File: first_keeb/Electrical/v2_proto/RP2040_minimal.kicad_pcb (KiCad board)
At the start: 2 copper layers, 54.3 x 61.2 mm, 32 parts, among them P1 USB_C_Receptacle_GCT_USB4105-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, Q1 SOT-23, SW1 2-1825027-0_Right_Angle_Switc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, U1 NCP1117-3.3_SOT223, U2 W25Q128JVS, U3 RP2040, U4 128x64OLED, Y1 ABLS-12.000MHZ-B4-T

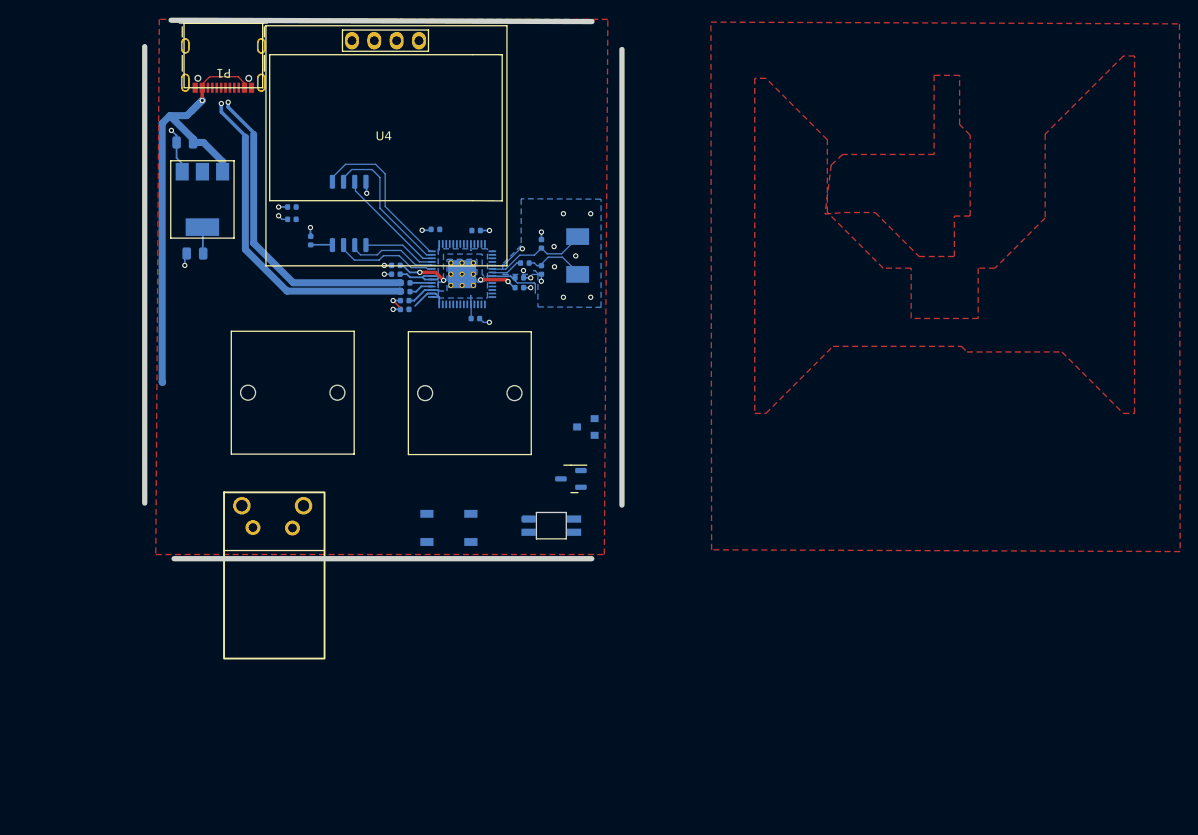
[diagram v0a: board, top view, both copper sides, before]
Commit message: finishes pcb except for the test points.
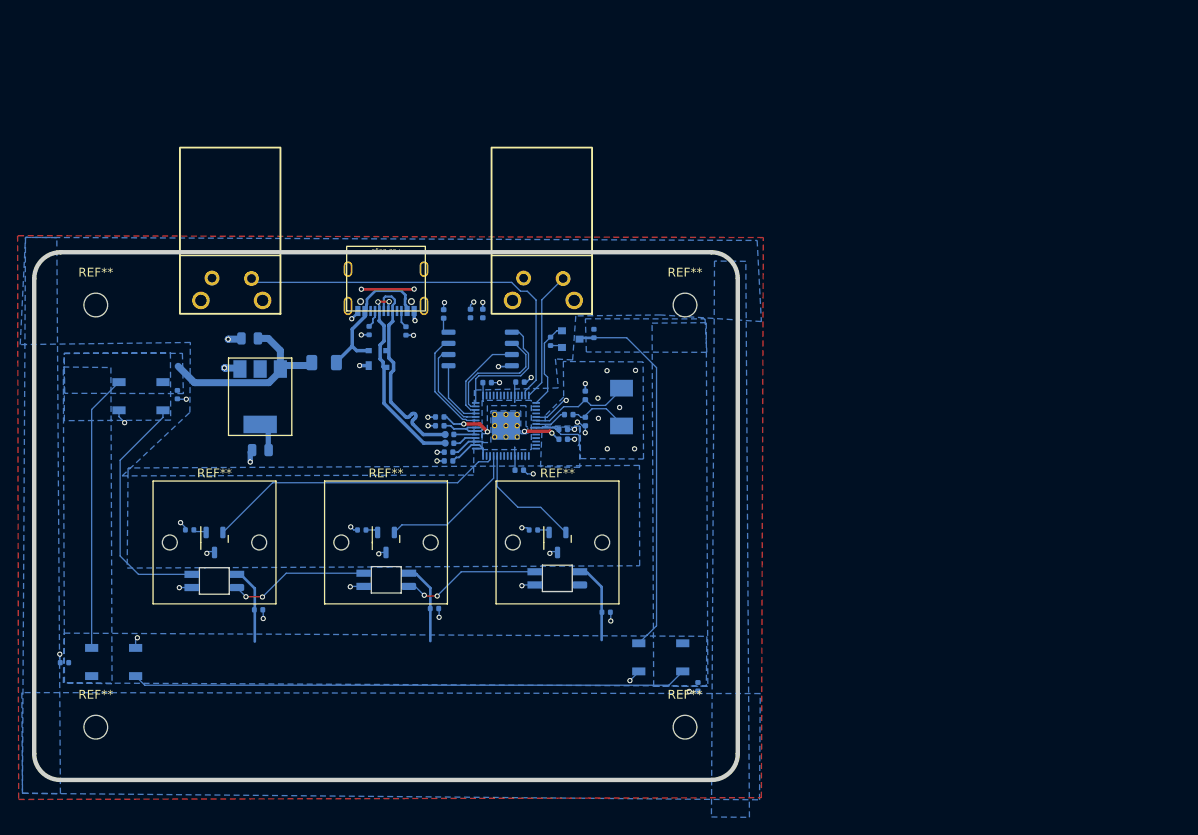
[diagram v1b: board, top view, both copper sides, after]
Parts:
- removed the REF** at (91.9, 107.9)
- removed the REF** at (112.1, 107.9)
- removed U4: 128x64OLED, SSD1306:128x64OLED
- added C19: C_0402_1005Metric, Capacitor_SMD:C_0402_1005Metric, B.Cu at (85.5, 137.7)
- added C20: C_0402_1005Metric, Capacitor_SMD:C_0402_1005Metric, B.Cu at (105.5, 137.5)
- added C21: C_0402_1005Metric, Capacitor_SMD:C_0402_1005Metric, B.Cu at (116.8, 128.6)
- added C22: C_0402_1005Metric, Capacitor_SMD:C_0402_1005Metric, B.Cu at (97.2, 128.6)
- added C23: C_0402_1005Metric, Capacitor_SMD:C_0402_1005Metric, B.Cu at (77.7, 128.6)
- added C24: C_0402_1005Metric, Capacitor_SMD:C_0402_1005Metric, B.Cu at (76.3, 113.2)
- added C25: C_0402_1005Metric, Capacitor_SMD:C_0402_1005Metric, B.Cu at (63.4, 143.7)
- added C26: C_0402_1005Metric, Capacitor_SMD:C_0402_1005Metric, B.Cu at (135.5, 146.4)
- added C28: C_0402_1005Metric, Capacitor_SMD:C_0402_1005Metric, B.Cu at (125.0, 137.9)
- added D2: SK6812-MINI-E, Keebio-Parts:SK6812-MINI-E, B.Cu at (100.0, 134.2)
- added D3: WS2812B, Keebio-Parts:WS2812B, B.Cu at (131.2, 143.1)
- added D4: WS2812B, Keebio-Parts:WS2812B, B.Cu at (69.0, 143.6)
- added D7: SK6812-MINI-E, Keebio-Parts:SK6812-MINI-E, B.Cu at (119.5, 134.1)
- added F1: Fuse_1206_3216Metric, Fuse:Fuse_1206_3216Metric, B.Cu at (93.0, 109.5)
- added R10: C_0402_1005Metric, Capacitor_SMD:C_0402_1005Metric, B.Cu at (123.6, 106.2)
- added R7: C_0402_1005Metric, Capacitor_SMD:C_0402_1005Metric, B.Cu at (98.1, 105.9)
- added R8: C_0402_1005Metric, Capacitor_SMD:C_0402_1005Metric, B.Cu at (102.3, 106.0)
- added R9: C_0402_1005Metric, Capacitor_SMD:C_0402_1005Metric, B.Cu at (118.7, 107.1)
- added REF**: SW_Lekker_MX_1.00u_PCB, Button_Switch_Keyboard:SW_Lekker_MX_1.00u_PCB, F.Cu at (80.5, 130.0)
- added REF**: SW_Lekker_MX_1.00u_PCB, Button_Switch_Keyboard:SW_Lekker_MX_1.00u_PCB, F.Cu at (119.5, 130.0)
- added REF**: SW_Lekker_MX_1.00u_PCB, Button_Switch_Keyboard:SW_Lekker_MX_1.00u_PCB, F.Cu at (100.0, 130.0)
- added REF**: MountingHole_2.7mm_M2.5, MountingHole:MountingHole_2.7mm_M2.5, F.Cu at (67.0, 103.0)
- added REF**: MountingHole_2.7mm_M2.5, MountingHole:MountingHole_2.7mm_M2.5, F.Cu at (67.0, 151.0)
- added REF**: MountingHole_2.7mm_M2.5, MountingHole:MountingHole_2.7mm_M2.5, F.Cu at (134.0, 103.0)
- added REF**: MountingHole_2.7mm_M2.5, MountingHole:MountingHole_2.7mm_M2.5, F.Cu at (134.0, 151.0)
- added S2: SS39ET, Package_TO_SOT_SMD:SOT-23-3, B.Cu at (100.0, 130.0)
- added S3: SS39ET, Package_TO_SOT_SMD:SOT-23-3, B.Cu at (80.5, 130.0)
- added SW2: 2-1825027-0_Right_Angle_Switch-9.24mm_Stem, Button_Switch_THT:2-1825027-0_Right_Angle_Button, F.Cu at (112.0, 104.0)
- added U5: SOT143B, Keebio-Parts:SOT-143B, B.Cu at (99.0, 109.1)
- P1: moved to B.Cu
- moved D1 38.8 mm to (80.5, 134.4), turned to 0 degrees
- moved D5 38.1 mm to (72.1, 113.4)
- moved P1 31.4 mm to (100.0, 100.0), turned to 0 degrees
- moved C16 24.9 mm to (111.0, 104.0), turned to 90 degrees
- moved C4 23.6 mm to (85.7, 119.5)
- moved C1 23.5 mm to (84.5, 106.8)
- moved U1 23.4 mm to (85.7, 113.4)
- moved C15 23.0 mm to (109.6, 104.0), turned to 90 degrees
- moved SW1 22.3 mm to (88.0, 104.0), turned to 180 degrees
- moved U2 21.4 mm to (110.7, 108.0), turned to 180 degrees
- moved C12 18.4 mm to (111.5, 111.8), turned to 0 degrees
- moved C10 17.9 mm to (107.1, 120.7)
- moved C11 17.9 mm to (115.2, 111.8)
- moved C13 17.9 mm to (115.2, 121.8)
- moved C14 17.9 mm to (120.1, 117.1)
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- renumbered D3 to D5
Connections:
- C1 pad 1: VBUS -> +5V
- D1 pad 1: (no net) -> DOUT_3
- D1 pad 2: (no net) -> GND
- D1 pad 3: (no net) -> DOUT_4
- D1 pad 4: (no net) -> +5V
- D5 pad 1: (no net) -> +5V
- D5 pad 2: (no net) -> DOUT_3
- D5 pad 3: (no net) -> GND
- D5 pad 4: (no net) -> DOUT_2
- P1 pad A5: (no net) -> CC1
- P1 pad B5: (no net) -> CC2
- P1 pad B6: (no net) -> /USB_D+
- P1 pad B7: (no net) -> /USB_D-
- P1 pad S1: GND -> (no net)
- Q1 pad 1: (no net) -> +3V3
- Q1 pad 2: (no net) -> /GPIO12
- Q1 pad 3: (no net) -> LED_D_5V
- S1 pad 1: (no net) -> +3V3
- S1 pad 2: (no net) -> /GPIO26_ADC0
- S1 pad 3: (no net) -> GND
- SW1 pad 1: (no net) -> /GPIO10
- SW1 pad 2: (no net) -> GND
- SW1 pad 3: (no net) -> GND
- SW1 pad 4: (no net) -> GND
- U1 pad 3: VBUS -> +5V
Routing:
- net DOUT_1: track 0.00 -> 63.3 mm
- net +5V: track 0.00 -> 49.1 mm
- net /GPIO10: track 0.00 -> 45.0 mm
- net LED_D_5V: track 0.00 -> 42.5 mm
- net VBUS: track 54.2 -> 17.6 mm, vias 1 -> 0
- net /GPIO28_ADC2: track 0.00 -> 34.2 mm
- net DOUT_2: track 0.00 -> 31.5 mm
- net DOUT_3: track 0.00 -> 27.6 mm
- net GND: track 29.0 -> 49.1 mm, vias 26 -> 50
- net /GPIO27_ADC1: track 0.00 -> 16.4 mm
- net DOUT_5: track 0.00 -> 16.1 mm, vias 0 -> 2
- net DOUT_4: track 0.00 -> 16.0 mm, vias 0 -> 2
- net /GPIO11: track 0.00 -> 14.9 mm
- net +3V3: track 28.9 -> 43.7 mm, vias 0 -> 2
- net /USB_D-: track 37.5 -> 23.5 mm, vias 1 -> 2
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- added copper zone on B.Cu, net +5V
- removed copper zone on F.Cu, net +3V3
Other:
- board size 54.3 x 61.2 mm -> 80 x 60 mm

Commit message: finishes proto_2 pcb
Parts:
- added D6: WS2812B, Keebio-Parts:WS2812B, B.Cu at (128.1, 106.4)
- added R5: C_0402_1005Metric, Capacitor_SMD:C_0402_1005Metric, B.Cu at (114.0, 104.5)
- added TP1: TestPoint_Pad_1.0x1.0mm, TestPoint:TestPoint_Pad_1.0x1.0mm, B.Cu at (116.4, 105.2)
- added TP2: RUN, TestPoint:TestPoint_Pad_1.0x1.0mm, B.Cu at (118.8, 122.1)
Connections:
- D3 pad 4: LED_D_5V -> DOUT_0
- P1 pad S1: (no net) -> GND
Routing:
- net LED_D_5V: track 42.5 -> 7.73 mm
- net DOUT_0: track 0.00 -> 34.3 mm
- net /RUN: track 0.00 -> 4.69 mm
- net /QSPI_SS: track 14.6 -> 18.7 mm
- net GND: track 49.1 -> 50.5 mm, vias 50 -> 51
- net DOUT_3: track 27.6 -> 28.3 mm

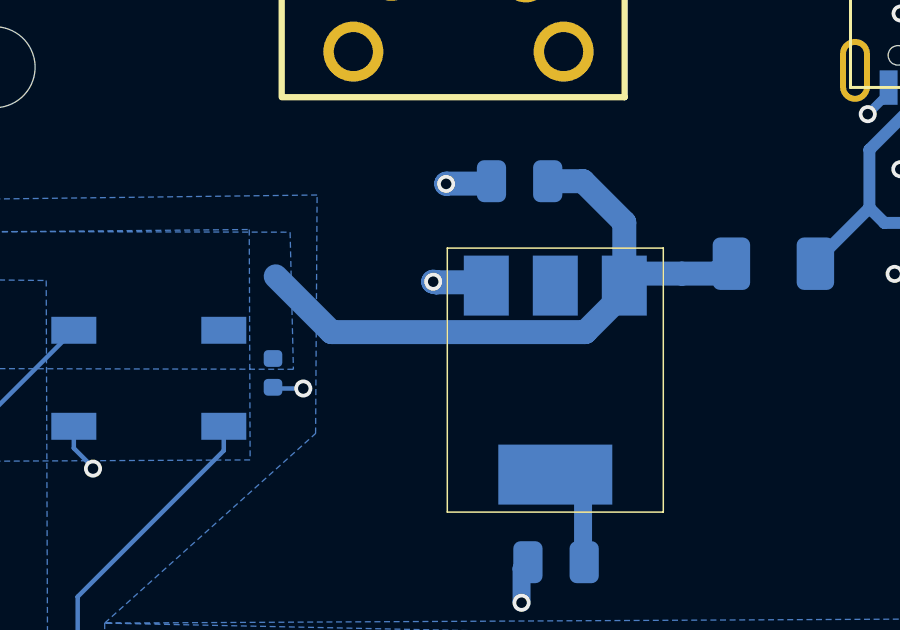
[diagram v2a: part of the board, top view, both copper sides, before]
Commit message: moves vbus away from pads
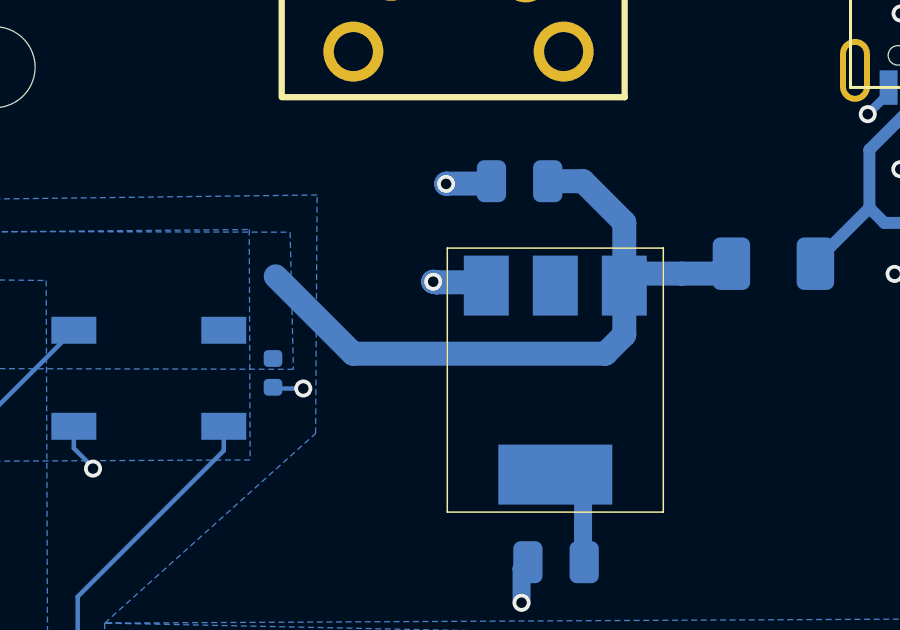
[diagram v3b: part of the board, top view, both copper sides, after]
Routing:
- net +5V: track 49.1 -> 50.5 mm
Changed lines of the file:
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@@
   (segment (start 86.615 106.8) (end 85.4375 106.8) (width 0.8) (layer "B.Cu") (net 54))
   (segment (start 105.04 135.18) (end 103.43 133.57) (width 0.3) (layer "B.Cu") (net 54))
-  (segment (start 76.37 109.97) (end 78.23 111.83) (width 0.8) (layer "B.Cu") (net 54))
   (segment (start 85.08 135.235) (end 83.47 133.625) (width 0.3) (layer "B.Cu") (net 54))
   (segment (start 91.23 109.88) (end 91.56 109.55) (width 0.8) (layer "B.Cu") (net 54))
   (segment (start 83.47 133.625) (end 83.03 133.625) (width 0.3) (layer "B.Cu") (net 54))
   (segment (start 89.91 109.88) (end 91.23 109.88) (width 0.8) (layer "B.Cu") (net 54))
-  (segment (start 78.23 111.83) (end 86.69 111.83) (width 0.8) (layer "B.Cu") (net 54))
+  (segment (start 76.37 109.97) (end 78.95 112.55) (width 0.8) (layer "B.Cu") (net 54))
   (segment (start 105.04 141.215) (end 105.04 135.18) (width 0.3) (layer "B.Cu") (net 54))
   (segment (start 133.73936 141.4598) (end 133.73936 141.39064) (width 0.15) (layer "B.Cu") (net 54))
-  (segment (start 87.99 110.53) (end 87.99 110.28) (width 0.8) (layer "B.Cu") (net 54))
-  (segment (start 86.69 111.83) (end 87.99 110.53) (width 0.8) (layer "B.Cu") (net 54))
+  (segment (start 87.36 112.55) (end 87.99 111.92) (width 0.8) (layer "B.Cu") (net 54))
   (segment (start 103.43 133.57) (end 102.99 133.57) (width 0.3) (layer "B.Cu") (net 54))
+  (segment (start 78.95 112.55) (end 87.36 112.55) (width 0.8) (layer "B.Cu") (net 54))
   (segment (start 90.89 109.6) (end 90.94 109.55) (width 0.15) (layer "B.Cu") (net 54))
   (segment (start 85.08 141.27) (end 85.08 135.235) (width 0.3) (layer "B.Cu") (net 54))
   (segment (start 86.615 106.8) (end 87.99 108.175) (width 0.8) (layer "B.Cu") (net 54))
+  (segment (start 87.99 111.92) (end 87.99 110.28) (width 0.8) (layer "B.Cu") (net 54))
   (segment (start 90.94 109.55) (end 91.56 109.55) (width 0.15) (layer "B.Cu") (net 54))
   (segment (start 87.99 108.175) (end 87.99 110.28) (width 0.8) (layer "B.Cu") (net 54))

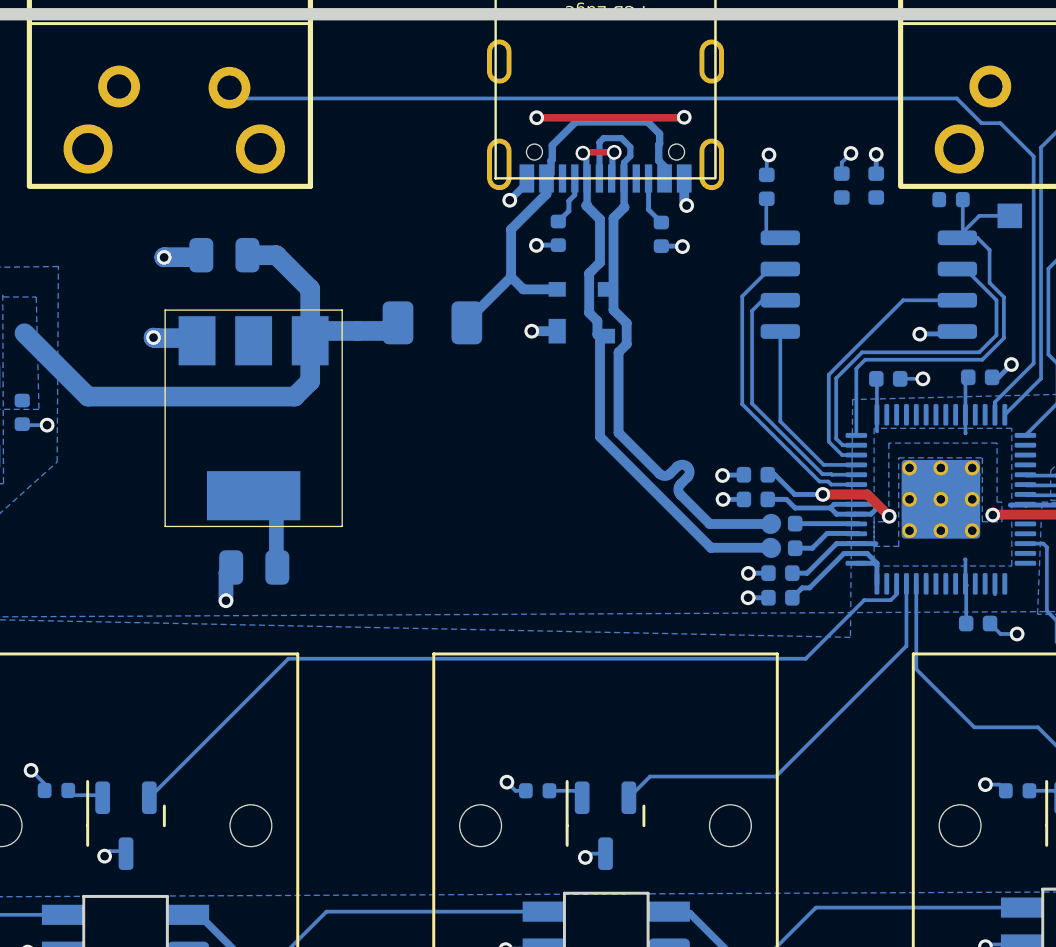
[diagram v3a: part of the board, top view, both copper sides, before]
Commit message: ads voltage reference
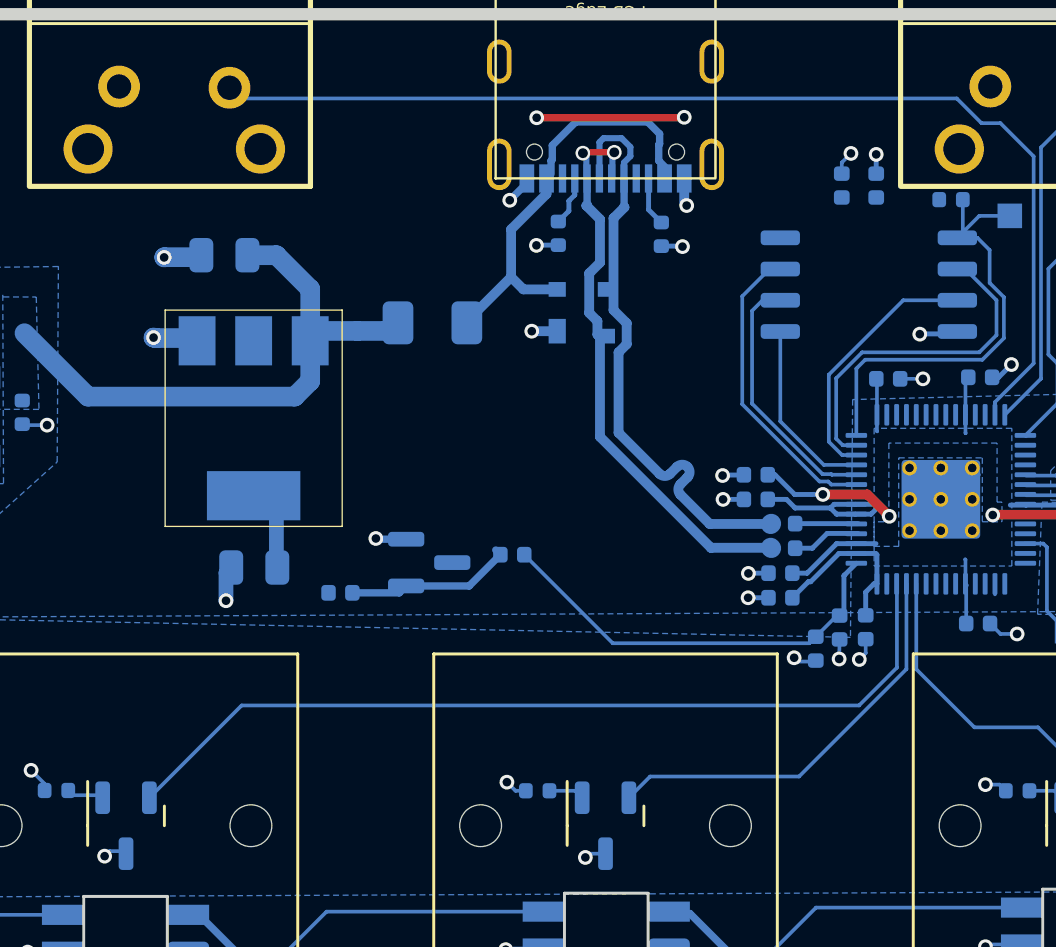
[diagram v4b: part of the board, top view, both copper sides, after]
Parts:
- added C14: 1u, Capacitor_SMD:C_0402_1005Metric, B.Cu at (108.5, 122.8)
- added C7: 100n, Capacitor_SMD:C_0402_1005Metric, B.Cu at (109.5, 121.9)
- added R1: 200R, Capacitor_SMD:C_0402_1005Metric, B.Cu at (89.2, 120.5)
- added R2: 1R, Capacitor_SMD:C_0402_1005Metric, B.Cu at (96.2, 119.0)
- added U2: SOT-23, Package_TO_SOT_SMD:SOT-23, B.Cu at (92.8, 119.3)
- C3: renamed from C13; value 100n -> 1u
- moved C5 18.4 mm to (110.6, 121.9), turned to -90 degrees
- renumbered C6 to C1, C1 to C10, C4 to C11, C8 to C12, C10 to C13, C2 to C17, C3 to C18, C7 to C2, C14 to C4, R5 to R6, U2 to U3
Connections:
- U3 pad 43: +3V3 -> ADC_AVDD
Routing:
- net ADC_AVDD: track 0.00 -> 16.9 mm
- net +3V: track 0.00 -> 6.93 mm
- net GND: track 50.5 -> 53.8 mm, vias 51 -> 54
- net /GPIO28_ADC2: track 34.2 -> 36.0 mm
- net +3V3: track 43.7 -> 43.0 mm
- net /GPIO27_ADC1: track 16.4 -> 16.9 mm
